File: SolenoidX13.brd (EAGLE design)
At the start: 24.3 x 25.4 mm, 26 parts, among them J1 SAMTEC-CLT-111-01-X-DJ, U1 ULN2003V12

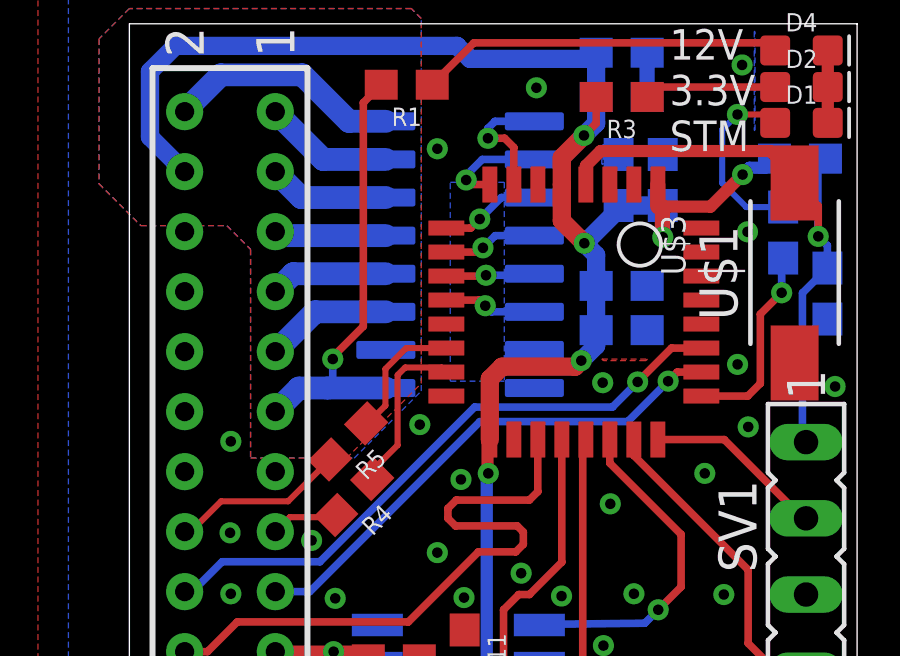
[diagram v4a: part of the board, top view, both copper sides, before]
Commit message: Added nrst pin to connector and routed
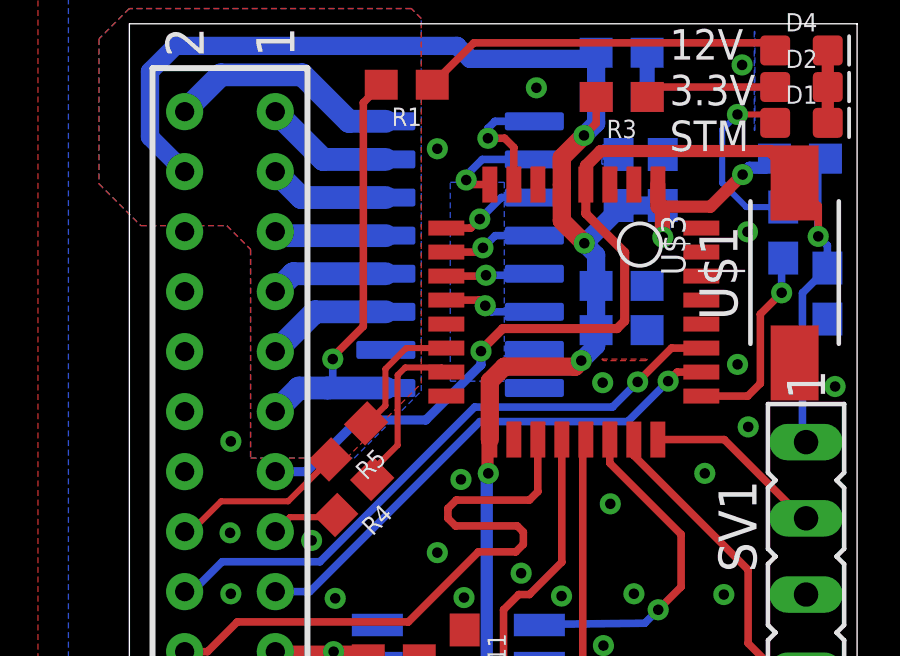
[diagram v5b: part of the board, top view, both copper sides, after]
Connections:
- net NRST: now also J1.13
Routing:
- net NRST: track 20.6 -> 39.7 mm, vias 1 -> 2
- net GND: vias 27 -> 26
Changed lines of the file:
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@@
 <via x="20.6022" y="18.4658" extent="1-16" drill="0.35"/>
 <via x="11.0518" y="10.2108" extent="1-16" drill="0.35"/>
-<via x="9.6802" y="12.0396" extent="1-16" drill="0.35"/>
 <via x="10.2644" y="21.2344" extent="1-16" drill="0.35"/>
 <via x="20.272" y="14.0462" extent="1-16" drill="0.35"/>
 <via x="15.7762" y="13.4366" extent="1-16" drill="0.35"/>
+<wire x1="20.4244" y1="24.0284" x2="23.2798" y2="24.511" width="0" layer="19" extent="1-1"/>
+<wire x1="17.2584" y1="24.4348" x2="20.4244" y2="24.0284" width="0" layer="19" extent="16-16"/>
+<wire x1="17.78" y1="21.043" x2="17.2584" y2="22.9616" width="0" layer="19" extent="16-16"/>
+<wire x1="16.3068" y1="21.043" x2="17.78" y2="21.043" width="0" layer="19" extent="16-16"/>
+<wire x1="19.0642" y1="18.5906" x2="17.78" y2="21.043" width="0" layer="19" extent="1-16"/>
+<wire x1="19.0642" y1="17.7906" x2="19.0642" y2="18.5906" width="0" layer="19" extent="1-1"/>
+<wire x1="20.6022" y1="18.4658" x2="19.0642" y2="18.5906" width="0" layer="19" extent="1-1"/>
+<wire x1="17.2584" y1="16.6624" x2="19.0642" y2="17.7906" width="0" layer="19" extent="1-16"/>
+<wire x1="17.2584" y1="15.1892" x2="17.2584" y2="16.6624" width="0" layer="19" extent="16-16"/>
+<wire x1="15.7762" y1="13.4366" x2="17.2584" y2="15.1892" width="0" layer="19" extent="16-16"/>
+<wire x1="13.4986" y1="13.2588" x2="15.7762" y2="13.4366" width="0" layer="19" extent="16-16"/>
+<wire x1="10.5642" y1="12.9906" x2="13.4986" y2="13.2588" width="0" layer="19" extent="1-16"/>
+<wire x1="11.0518" y1="10.2108" x2="10.5642" y2="12.9906" width="0" layer="19" extent="1-1"/>
+<wire x1="10.2644" y1="7.7724" x2="11.0518" y2="10.2108" width="0" layer="19" extent="1-1"/>
+<wire x1="11.1534" y1="6.2738" x2="10.2644" y2="7.7724" width="0" layer="19" extent="1-1"/>
+<wire x1="11.176" y1="5.1934" x2="11.1534" y2="6.2738" width="0" layer="19" extent="1-1"/>
+<wire x1="13.0584" y1="7.0866" x2="11.1534" y2="6.2738" width="0" layer="19" extent="1-1"/>
+<wire x1="14.4046" y1="6.3246" x2="13.0584" y2="7.0866" width="0" layer="19" extent="1-1"/>
+<wire x1="15.8016" y1="4.6736" x2="14.4046" y2="6.3246" width="0" layer="19" extent="1-1"/>
+<wire x1="16.8176" y1="6.4008" x2="15.8016" y2="4.6736" width="0" layer="19" extent="1-1"/>
+<wire x1="13.6652" y1="4.0894" x2="15.8016" y2="4.6736" width="0" layer="19" extent="16-16"/>
+<wire x1="19.8148" y1="6.3754" x2="16.8176" y2="6.4008" width="0" layer="19" extent="1-1"/>
+<wire x1="22.5552" y1="6.3754" x2="19.8148" y2="6.3754" width="0" layer="19" extent="1-1"/>
+<wire x1="16.0302" y1="9.398" x2="16.8176" y2="6.4008" width="0" layer="19" extent="1-1"/>
+<wire x1="20.272" y1="14.0462" x2="17.2584" y2="15.1892" width="0" layer="19" extent="16-16"/>
+<wire x1="22.1742" y1="14.0942" x2="20.272" y2="14.0462" width="0" layer="19" extent="1-1"/>
+<wire x1="23.5232" y1="13.3096" x2="22.1742" y2="14.0942" width="0" layer="19" extent="1-1"/>
+<wire x1="23.2664" y1="15.5584" x2="22.1742" y2="14.0942" width="0" layer="19" extent="1-16"/>
+<wire x1="20.6276" y1="11.9634" x2="20.272" y2="14.0462" width="0" layer="19" extent="1-1"/>
+<wire x1="19.1798" y1="10.414" x2="20.6276" y2="11.9634" width="0" layer="19" extent="1-1"/>
+<wire x1="13.5664" y1="23.2664" x2="16.3068" y2="21.043" width="0" layer="19" extent="16-16"/>
+<wire x1="15.0142" y1="0.762" x2="13.6652" y2="4.0894" width="0" layer="19" extent="16-16"/>
+<wire x1="16.3576" y1="1.1058" x2="15.0142" y2="0.762" width="0" layer="19" extent="16-16"/>
+<wire x1="6.8608" y1="6.2484" x2="10.2644" y2="7.7724" width="0" layer="19" extent="1-1"/>
+<wire x1="6.0734" y1="8.1788" x2="6.8608" y2="6.2484" width="0" layer="19" extent="1-1"/>
+<wire x1="3.3556" y1="8.4328" x2="6.0734" y2="8.1788" width="0" layer="19" extent="1-1"/>
+<wire x1="3.381" y1="6.4008" x2="3.3556" y2="8.4328" width="0" layer="19" extent="1-1"/>
+<wire x1="6.2484" y1="3.4318" x2="6.8608" y2="6.2484" width="0" layer="19" extent="1-1"/>
+<wire x1="3.381" y1="11.4808" x2="3.3556" y2="8.4328" width="0" layer="19" extent="1-1"/>
+<wire x1="1.8418" y1="12.4714" x2="3.381" y2="11.4808" width="0" layer="19" extent="1-1"/>
+<wire x1="1.8418" y1="14.4714" x2="1.8418" y2="12.4714" width="0" layer="19" extent="1-1"/>
+<wire x1="1.8418" y1="16.4714" x2="1.8418" y2="14.4714" width="0" layer="19" extent="1-1"/>
+<wire x1="1.8418" y1="18.4714" x2="1.8418" y2="16.4714" width="0" layer="19" extent="1-1"/>
+<wire x1="10.2644" y1="21.2344" x2="13.5664" y2="23.2664" width="0" layer="19" extent="1-1"/>
+<wire x1="0.8918" y1="1.1176" x2="6.2484" y2="3.4318" width="0" layer="19" extent="1-1"/>
 </signal>
 <signal name="+3V3">
@@
 <wire x1="15.5584" y1="22.0832125" x2="15.15259375" y2="21.67740625" width="0.254" layer="1"/>
 <wire x1="17.78" y1="19.343" x2="16.3068" y2="19.343" width="0.6096" layer="16"/>
-<wire x1="12.0142" y1="11.5406" x2="12.0142" y2="13.5636" width="0.6096" layer="1"/>
+<wire x1="12.0142" y1="11.5406" x2="12.0142" y2="13.4874" width="0.6096" layer="1"/>
 <wire x1="15.0622" y1="14.1732" x2="14.859" y2="13.97" width="0.6096" layer="1"/>
-<wire x1="14.859" y1="13.97" x2="12.4206" y2="13.97" width="0.6096" layer="1"/>
+<wire x1="14.859" y1="13.97" x2="12.4968" y2="13.97" width="0.6096" layer="1"/>
 <via x="15.0622" y="14.1732" extent="1-16" drill="0.35"/>
-<wire x1="12.0142" y1="13.5636" x2="12.4206" y2="13.97" width="0.6096" layer="1"/>
+<wire x1="12.0142" y1="13.4874" x2="12.4968" y2="13.97" width="0.6096" layer="1"/>
 <wire x1="15.5584" y1="15.1892" x2="15.5584" y2="14.6694" width="0.6096" layer="16"/>
 <wire x1="15.5584" y1="14.6694" x2="15.0622" y2="14.1732" width="0.6096" layer="16"/>
@@
 <wire x1="22.4362" y1="16.4282" x2="22.4362" y2="11.5744" width="0.254" layer="16"/>
 <wire x1="22.4362" y1="16.4282" x2="23.2664" y2="17.2584" width="0.254" layer="16"/>
+<wire x1="15.2142" y1="20.0406" x2="15.2142" y2="19.0758" width="0.3048" layer="1"/>
+<wire x1="16.51" y1="15.494" x2="16.256" y2="15.24" width="0.3048" layer="1"/>
+<wire x1="16.256" y1="15.24" x2="12.446" y2="15.24" width="0.3048" layer="1"/>
+<wire x1="12.446" y1="15.24" x2="11.7202" y2="14.5142" width="0.3048" layer="1"/>
+<wire x1="11.7202" y1="14.5142" x2="11.7202" y2="14.48695625" width="0.3048" layer="1"/>
+<via x="11.7202" y="14.48695625" extent="1-16" drill="0.35"/>
+<wire x1="15.2142" y1="19.0758" x2="16.51" y2="17.78" width="0.3048" layer="1"/>
+<wire x1="16.51" y1="17.78" x2="16.51" y2="15.494" width="0.3048" layer="1"/>
+<contactref element="J1" pad="13"/>
+<wire x1="4.8638" y1="10.4714" x2="5.8994" y2="10.4714" width="0.3048" layer="16"/>
+<wire x1="11.7202" y1="14.02975625" x2="9.88244375" y2="12.192" width="0.3048" layer="16"/>
+<wire x1="11.7202" y1="14.02975625" x2="11.7202" y2="14.48695625" width="0.3048" layer="16"/>
+<wire x1="5.8994" y1="10.4714" x2="7.62" y2="12.192" width="0.3048" layer="16"/>
+<wire x1="7.62" y1="12.192" x2="9.88244375" y2="12.192" width="0.3048" layer="16"/>
 </signal>
 <signal name="N$1">

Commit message: smol changes
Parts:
- moved U$8 0.89 mm to (12.8, 1.60)
- moved C11 0.81 mm to (10.4, 4.17)
- moved R10 0.69 mm to (8.13, 4.27)
- moved R11 0.69 mm to (8.13, 2.79)
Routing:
- net CAN_TX: track 11.1 -> 12.0 mm
- net CAN_H: track 4.82 -> 3.99 mm
- net CAN_L: track 4.81 -> 4.09 mm
- net GND: vias 26 -> 27
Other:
- board text added: "X13 Solenoid 01/01/2021 Erin Park Katherine Sandys Grant Geyer"
- board text removed: "ROV X13 Solenoid 12/04/2020 Erin Park Katherine Sandys Grant Geyer"

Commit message: added an OWO
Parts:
- moved C11 0.10 mm to (10.5, 4.17)
- renumbered U$1 to RESET, U$3 to STM
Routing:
- net GND: vias 27 -> 26
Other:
- board text added: "(◕ ྌ ◕✿)✧･ﾟ: *"

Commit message: ground plane? more like ground pain
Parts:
- moved R4 2.37 mm to (8.13, 11.9), turned to 270 degrees
- moved R5 0.64 mm to (6.65, 11.4), turned to 270 degrees
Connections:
- net GND: no longer J1.12
- net SWCLK: now also J1.12
- net SWDIO: now also J1.14
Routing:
- net SWDIO: track 6.03 -> 41.8 mm, vias 0 -> 1
- net SWCLK: track 10.7 -> 33.2 mm, vias 0 -> 2
- net GND: track 3.89 -> 23.7 mm, vias 26 -> 27
- net 12V: track 14.9 -> 19.3 mm, vias 1 -> 2
- net N$1: track 5.60 -> 3.03 mm
- net C2_2: track 2.26 -> 4.64 mm
- net N$2: track 4.43 -> 5.93 mm
